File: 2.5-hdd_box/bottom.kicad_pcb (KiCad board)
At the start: 2 copper layers, 120 x 105.4 mm, 13 parts

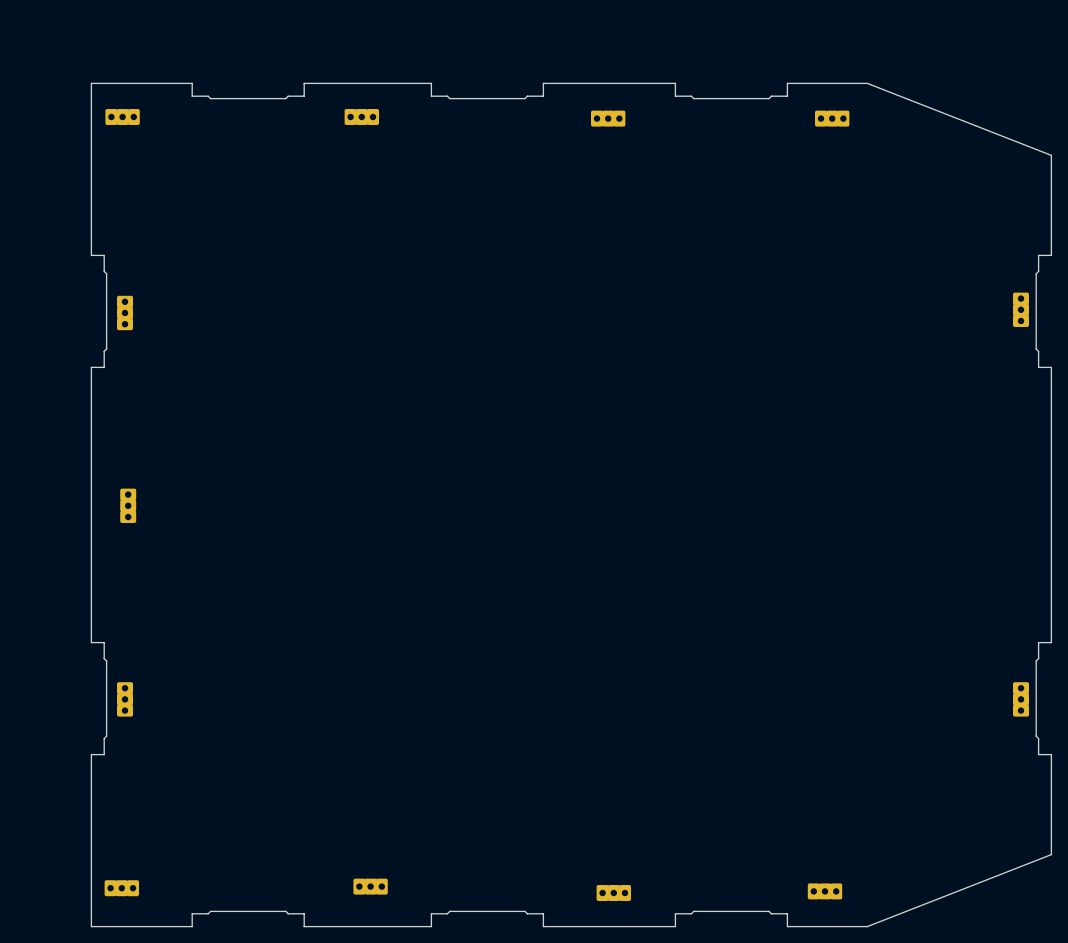
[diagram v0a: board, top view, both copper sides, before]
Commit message: 2.5-hdd_box: cut on bottom for usb-sata board, better placement of soldier pads
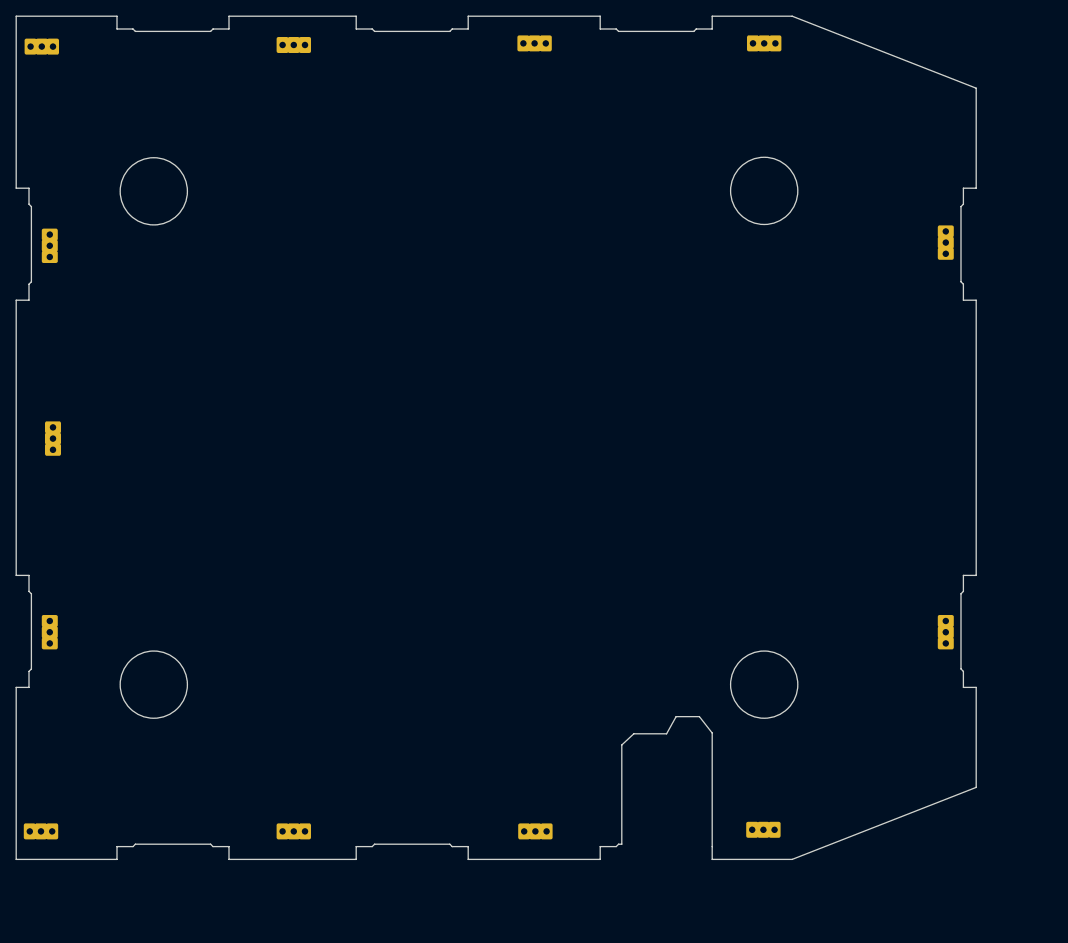
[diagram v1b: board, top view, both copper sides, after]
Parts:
- removed the REF** at (60.1, 92.0)
- removed the REF** at (148.2, 43.7)
- removed the REF** at (59.4, 139.9)
- removed the REF** at (171.7, 67.5)
- removed the REF** at (90.5, 139.7)
- removed the REF** at (120.2, 43.7)
- removed the REF** at (59.7, 67.9)
- removed the REF** at (89.4, 43.5)
- removed the REF** at (59.5, 43.5)
- removed the REF** at (59.7, 116.2)
- removed the REF** at (171.7, 116.2)
- removed the REF** at (147.3, 140.3)
- removed the REF** at (120.9, 140.5)
- added ?: , , F.Cu at (139.6, 114.5)
- added ?: , , F.Cu at (139.6, 52.7)
- added ?: , , F.Cu at (63.3, 114.5)
- added REF**: soldpad, Local:soldpad, F.Cu at (49.3, 132.8)
- added REF**: soldpad, Local:soldpad, F.Cu at (80.9, 132.8)
- added REF**: soldpad, Local:soldpad, F.Cu at (50.3, 59.5)
- added REF**: soldpad, Local:soldpad, F.Cu at (111.0, 34.3)
- added REF**: soldpad, Local:soldpad, F.Cu at (139.6, 132.6)
- added REF**: soldpad, Local:soldpad, F.Cu at (162.3, 59.1)
- added REF**: soldpad, Local:soldpad, F.Cu at (50.7, 83.6)
- added REF**: soldpad, Local:soldpad, F.Cu at (50.3, 107.8)
- added REF**: soldpad, Local:soldpad, F.Cu at (80.9, 34.5)
- added REF**: soldpad, Local:soldpad, F.Cu at (139.7, 34.3)
- added REF**: soldpad, Local:soldpad, F.Cu at (49.4, 34.7)
- added REF**: soldpad, Local:soldpad, F.Cu at (111.1, 132.8)
- added REF**: soldpad, Local:soldpad, F.Cu at (162.3, 107.8)
- added REF**: MountingHole_8.4mm_M8, MountingHole:MountingHole_8.4mm_M8, F.Cu at (63.3, 52.8)
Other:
- outline, holes or cut-outs redrawn
- board text added: "Bottom"

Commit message: Cosmetic changes
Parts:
- added ?: , , F.Cu at (156.7, 68.3)
- added ?: , , F.Cu at (156.6, 108.7)
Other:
- board text added: "T10000/T10K size box for 2.5'' HDD size is not too far from the IBM Jaguar 3592 v0.1"
- board text added: "https://github.com/saitis-net/sl8500_retrofit_electronics/tree/main/2.5-hdd_box"

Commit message: last order has small mistakes, this one should be better. Other things added, your responsibility to discover
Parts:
- removed the REF** at (80.9, 132.8)
- removed the REF** at (50.3, 59.5)
- removed the REF** at (162.3, 59.1)
- removed the REF** at (50.7, 83.6)
- removed the REF** at (50.3, 107.8)
- removed the REF** at (80.9, 34.5)
- removed the REF** at (162.3, 107.8)
- added ?: , , F.Cu at (78.3, 39.9)
- added ?: , , F.Cu at (157.9, 83.6)
- added ?: , , F.Cu at (139.7, 127.3)
- added ?: , , F.Cu at (78.3, 127.3)
- added ?: , , F.Cu at (139.7, 39.9)
- added REF**: soldpad, Local:soldpad, F.Cu at (162.4, 59.1)
- added REF**: soldpad, Local:soldpad, F.Cu at (78.5, 133.1)
- added REF**: soldpad, Local:soldpad, F.Cu at (49.2, 83.7)
- added REF**: soldpad, Local:soldpad, F.Cu at (162.6, 107.8)
- added REF**: soldpad, Local:soldpad, F.Cu at (78.5, 34.3)
- added REF**: soldpad, Local:soldpad, F.Cu at (49.3, 59.4)
- added REF**: soldpad, Local:soldpad, F.Cu at (49.3, 107.8)
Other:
- outline, holes or cut-outs redrawn
- board text added: "T10000/T10K size box for 2.5'' HDD size is not too far from the IBM Jaguar 3592 v0.2"
- board text removed: "T10000/T10K size box for 2.5'' HDD size is not too far from the IBM Jaguar 3592 v0.1"
